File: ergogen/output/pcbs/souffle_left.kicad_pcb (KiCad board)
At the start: 2 copper layers, 167.8 x 99.4 mm, 108 parts

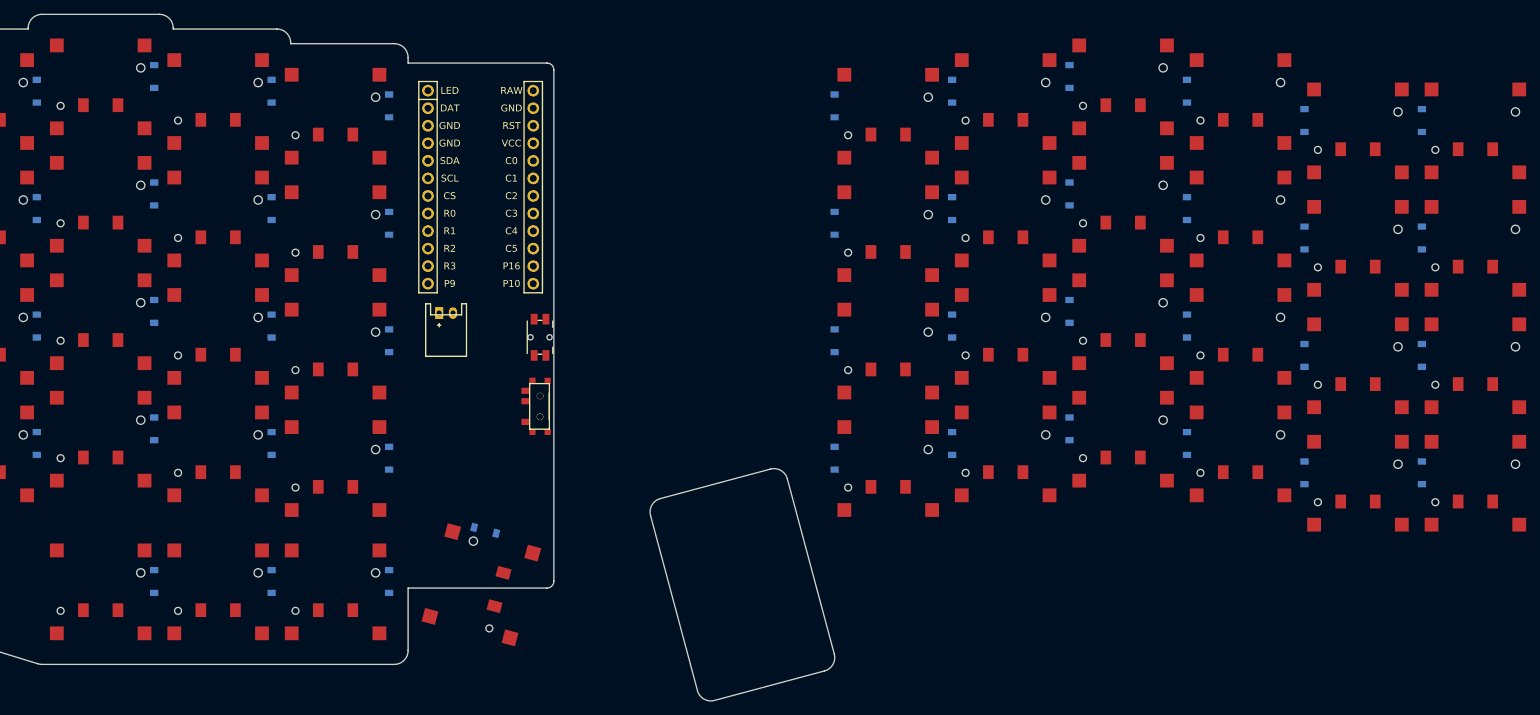
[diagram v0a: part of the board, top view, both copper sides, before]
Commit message: feat: both hands working
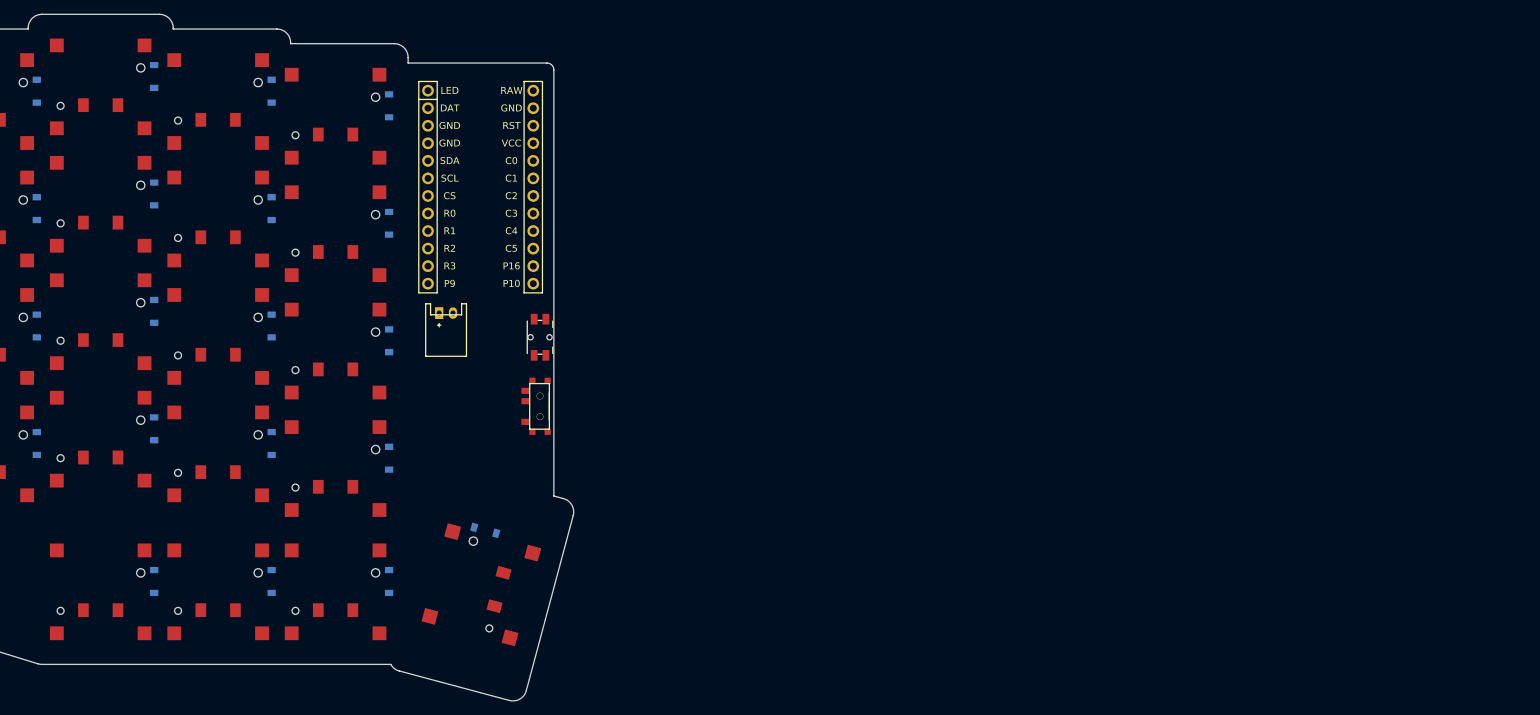
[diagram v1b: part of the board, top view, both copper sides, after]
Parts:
- removed D29, D30, D31, D32, D33, D34, D35, D36, D37, D38, D39, D40, D41, D42, D43, D44, D45, D46, D47, D48, D49, D50, D51, D52: , ceoloide:diode_tht_sod123
- removed S29, S30, S31, S32, S33, S34, S35, S36, S37, S38, S39, S40, S41, S42, S43, S44, S45, S46, S47, S48, S49, S50, S51, S52: , CPG1316S01D02_mikeholscher
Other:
- board size 167.8 x 99.4 mm -> 130 x 99.4 mm

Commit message: feat: choc version
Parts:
- S1, S10, S11, S12, S13, S14, S15, S16, S17, S18, S19, S2, S20, S21, S22, S23, S24, S25, S26, S27, S28, S3, S4, S5, S6, S7, S8, S9: footprint CPG1316S01D02_mikeholscher -> ceoloide:switch_choc_v1_v2; moved to B.Cu
- moved D28 9.38 mm to (216.0, 107.3), turned to -15 degrees
- moved S28 9.38 mm to (215.5, 115.2), turned to 255 degrees
- moved D24 7.66 mm to (200.2, 43.8), turned to -90 degrees
- moved MCU1 7.66 mm to (213.5, 54.3)
- moved S24 7.66 mm to (192.5, 45.3), turned to 180 degrees
- moved D23 7.57 mm to (200.2, 61.3), turned to -90 degrees
- moved S23 7.57 mm to (192.5, 62.8), turned to 180 degrees
- moved B1 7.52 mm to (222.1, 78.3)
- moved D22 7.52 mm to (200.2, 78.8), turned to -90 degrees
- moved JST1 7.52 mm to (208.5, 74.8)
- moved S22 7.52 mm to (192.5, 80.3), turned to 180 degrees
- moved T1 7.52 mm to (222.1, 88.3)
- moved D27 7.51 mm to (200.2, 114.7), turned to -90 degrees
- moved S27 7.51 mm to (192.5, 116.2), turned to 180 degrees
- moved D21 7.50 mm to (200.2, 96.3), turned to -90 degrees
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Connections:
- S1 pad 1: outer_bottom -> C0
- S1 pad 2: C0 -> outer_bottom
- S10 pad 1: ring_home -> C2
- S10 pad 2: C2 -> ring_home
- S11 pad 1: ring_top -> C2
- S11 pad 2: C2 -> ring_top
- S12 pad 1: ring_number -> C2
- S12 pad 2: C2 -> ring_number
- S13 pad 1: middle_bottom -> C3
- S13 pad 2: C3 -> middle_bottom
- S14 pad 1: middle_home -> C3
- S14 pad 2: C3 -> middle_home
- S15 pad 1: middle_top -> C3
- S15 pad 2: C3 -> middle_top
- S16 pad 1: middle_number -> C3
- S16 pad 2: C3 -> middle_number
- S17 pad 1: index_bottom -> C4
- S17 pad 2: C4 -> index_bottom
- S18 pad 1: index_home -> C4
- S18 pad 2: C4 -> index_home
- S19 pad 1: index_top -> C4
- S19 pad 2: C4 -> index_top
- S2 pad 1: outer_home -> C0
- S2 pad 2: C0 -> outer_home
- S20 pad 1: index_number -> C4
- S20 pad 2: C4 -> index_number
- S21 pad 1: inner_bottom -> C5
- S21 pad 2: C5 -> inner_bottom
- S22 pad 1: inner_home -> C5
- S22 pad 2: C5 -> inner_home
- S23 pad 1: inner_top -> C5
- S23 pad 2: C5 -> inner_top
- S24 pad 1: inner_number -> C5
- S24 pad 2: C5 -> inner_number
- S25 pad 1: inward_home -> C2
- S25 pad 2: C2 -> inward_home
- S26 pad 1: outward_home -> C3
- S26 pad 2: C3 -> outward_home
- S27 pad 1: small_thumbkey_home -> C4
- S27 pad 2: C4 -> small_thumbkey_home
- S28 pad 1: thumbkey_home -> C5
- S28 pad 2: C5 -> thumbkey_home
- S3 pad 1: outer_top -> C0
- S3 pad 2: C0 -> outer_top
- S4 pad 1: outer_number -> C0
- S4 pad 2: C0 -> outer_number
- S5 pad 1: pinky_bottom -> C1
- S5 pad 2: C1 -> pinky_bottom
- S6 pad 1: pinky_home -> C1
- S6 pad 2: C1 -> pinky_home
- S7 pad 1: pinky_top -> C1
- S7 pad 2: C1 -> pinky_top
- S8 pad 1: pinky_number -> C1
- S8 pad 2: C1 -> pinky_number
- S9 pad 1: ring_bottom -> C2
- S9 pad 2: C2 -> ring_bottom
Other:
- board size 130 x 99.4 mm -> 140.1 x 101.8 mm

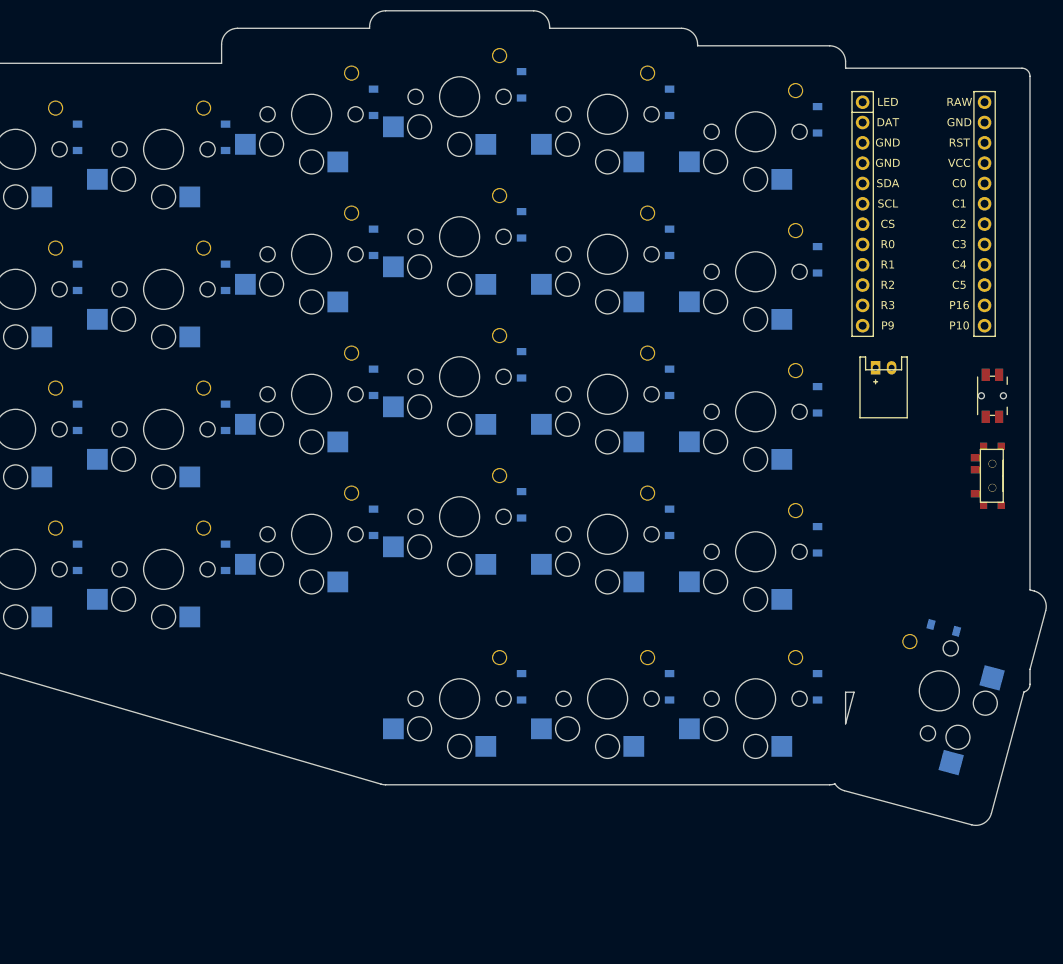
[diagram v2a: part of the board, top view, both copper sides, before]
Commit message: feat: moved mcu to the back and shortened its supporting tab
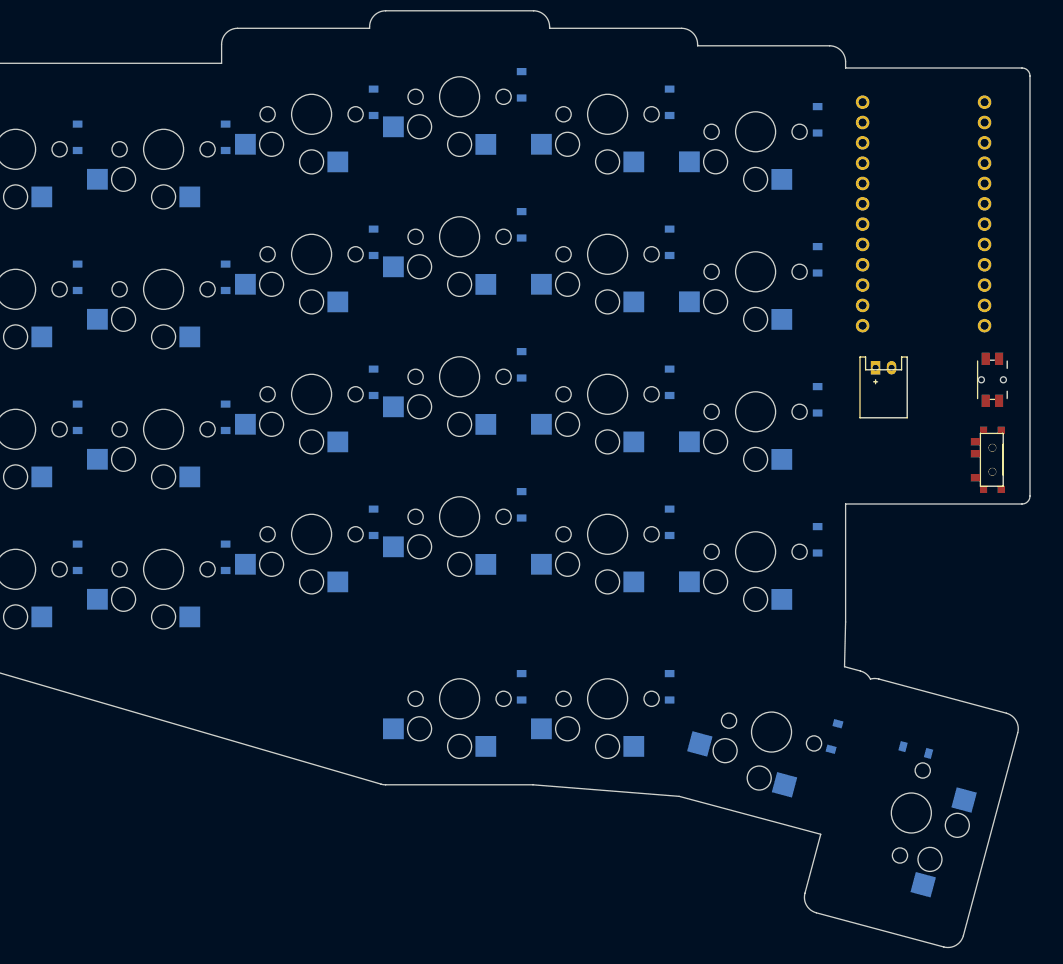
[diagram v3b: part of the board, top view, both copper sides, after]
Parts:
- MCU1: moved to B.Cu
- moved D28 15.7 mm to (212.5, 122.6)
- moved S28 15.7 mm to (212.0, 130.5)
- moved D27 6.56 mm to (202.4, 120.9), turned to -105 degrees
- moved S27 4.61 mm to (194.5, 120.3), turned to 165 degrees
- moved B1 2.00 mm to (222.1, 76.3)
- moved T1 2.00 mm to (222.1, 86.3)
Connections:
- MCU1 pad 1: RAW -> LED
- MCU1 pad 10: C5 -> R2
- MCU1 pad 11: P16 -> R3
- MCU1 pad 12: P10 -> P9
- MCU1 pad 13: P9 -> P10
- MCU1 pad 14: R3 -> P16
- MCU1 pad 15: R2 -> C5
- MCU1 pad 16: R1 -> C4
- MCU1 pad 17: R0 -> C3
- MCU1 pad 18: CS -> C2
- MCU1 pad 19: SCL -> C1
- MCU1 pad 2: GND -> DAT
- MCU1 pad 20: SDA -> C0
- MCU1 pad 21: GND -> VCC
- MCU1 pad 22: GND -> RST
- MCU1 pad 23: DAT -> GND
- MCU1 pad 24: LED -> RAW
- MCU1 pad 3: RST -> GND
- MCU1 pad 4: VCC -> GND
- MCU1 pad 5: C0 -> SDA
- MCU1 pad 6: C1 -> SCL
- MCU1 pad 7: C2 -> CS
- MCU1 pad 8: C3 -> R0
- MCU1 pad 9: C4 -> R1
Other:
- board size 140.1 x 101.8 mm -> 138 x 117.1 mm

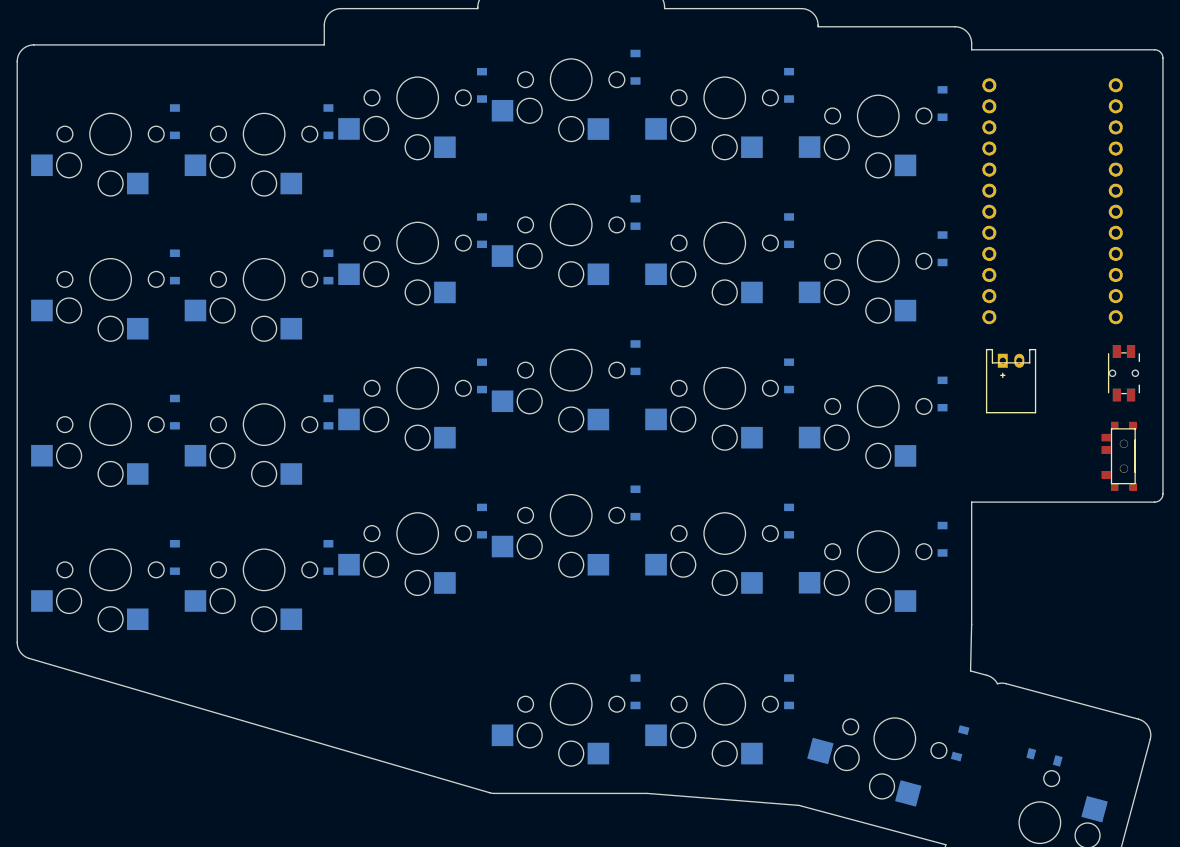
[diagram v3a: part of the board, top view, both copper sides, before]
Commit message: feat: left hand mcu and buttons on the back
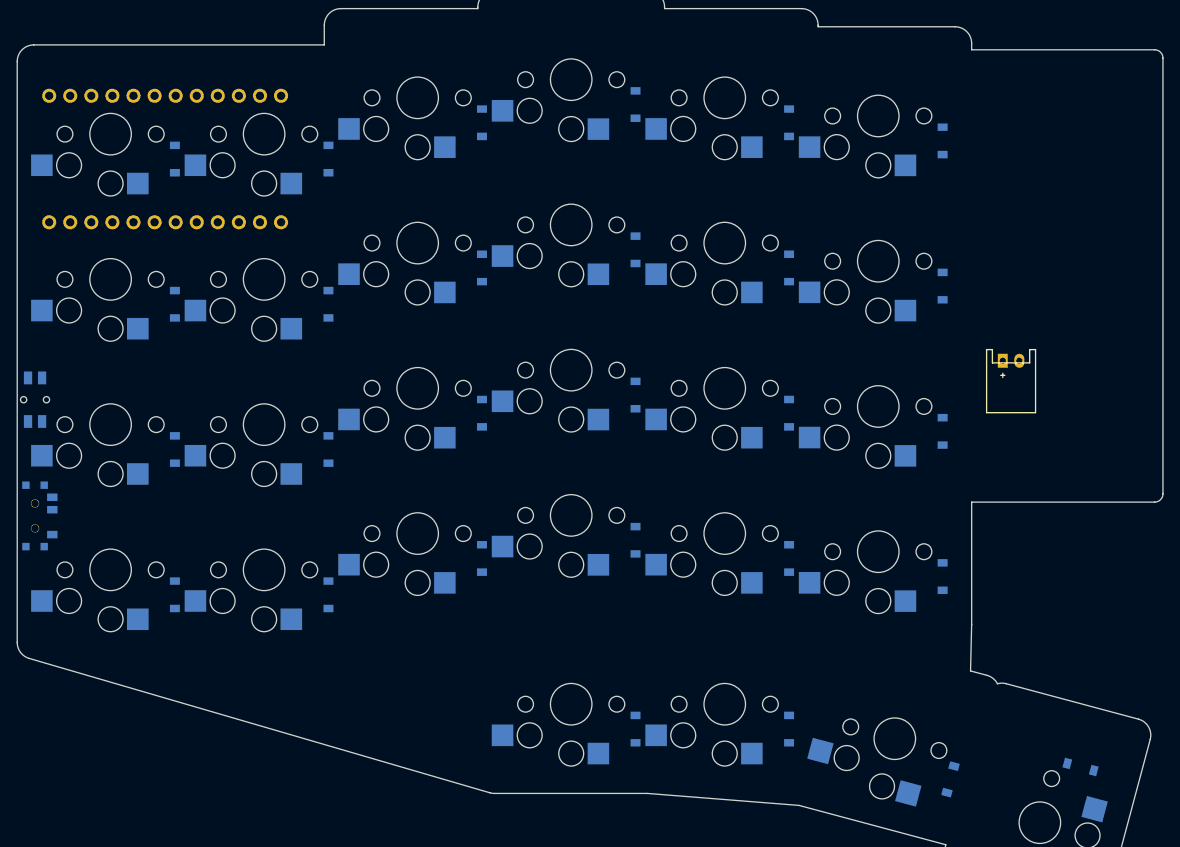
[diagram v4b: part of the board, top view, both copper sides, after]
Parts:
- moved T1 131.4 mm to (90.9, 93.5), turned to 90 degrees
- moved B1 131.2 mm to (90.9, 79.5), turned to 90 degrees
- moved MCU1 108.3 mm to (105.3, 50.5), turned to 90 degrees
- moved D1 4.50 mm to (107.8, 103.0)
- moved D10 4.50 mm to (144.8, 81.1)
- moved D11 4.50 mm to (144.8, 63.6)
- moved D12 4.50 mm to (144.8, 46.1)
- moved D13 4.50 mm to (163.2, 96.4)
- moved D14 4.50 mm to (163.2, 78.9)
- moved D15 4.50 mm to (163.2, 61.4)
- moved D16 4.50 mm to (163.2, 43.9)
- moved D17 4.50 mm to (181.8, 98.6)
- moved D18 4.50 mm to (181.8, 81.1)
- moved D19 4.50 mm to (181.8, 63.6)
- moved D2 4.50 mm to (107.8, 85.5)
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
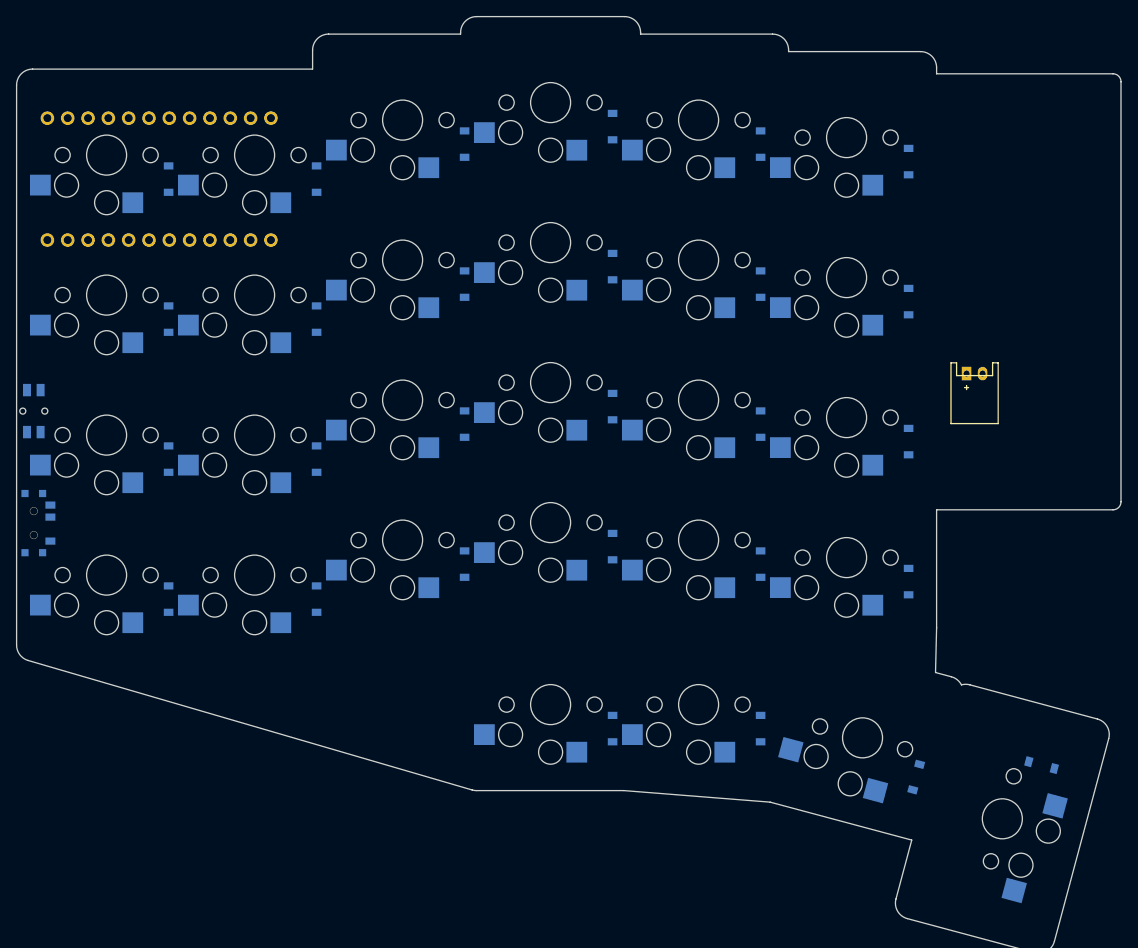
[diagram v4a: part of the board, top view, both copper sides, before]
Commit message: feat: mcu and buttons positioning for the right hand
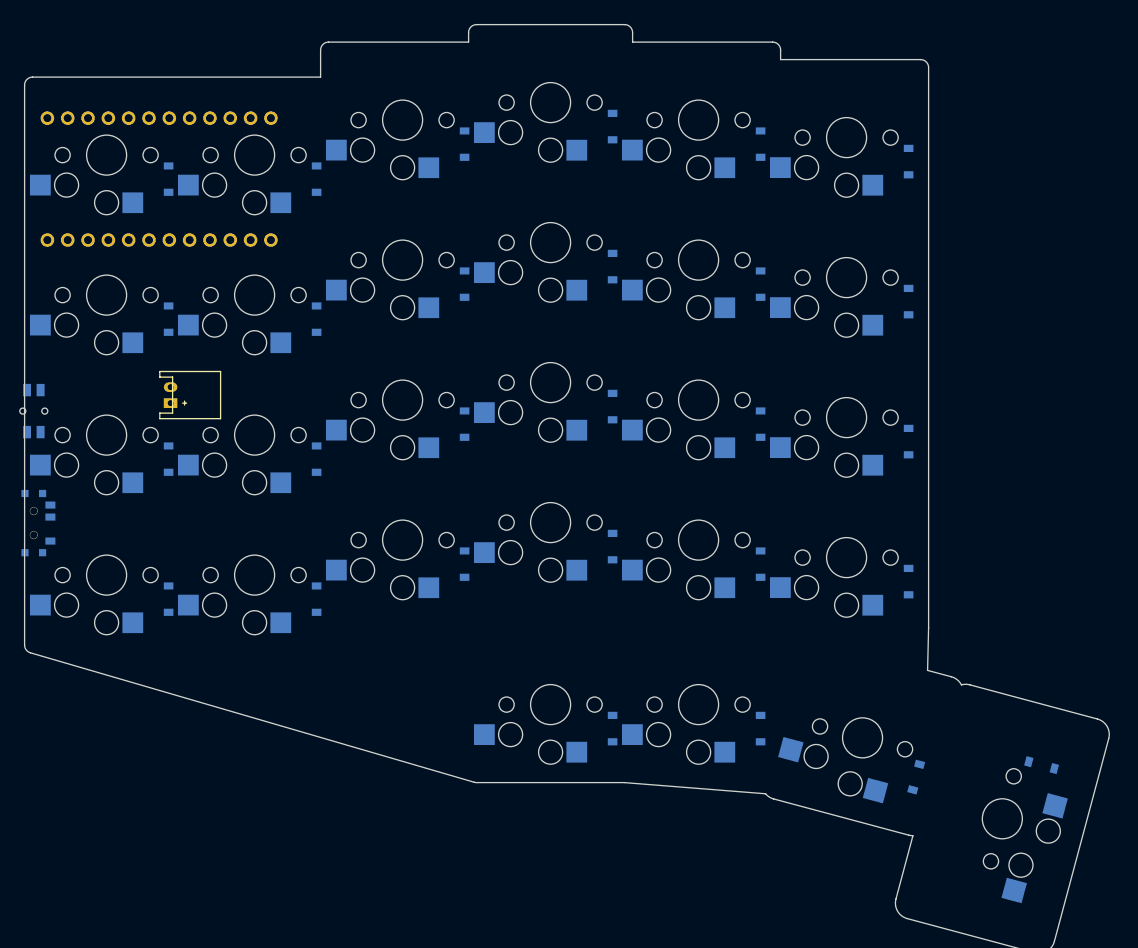
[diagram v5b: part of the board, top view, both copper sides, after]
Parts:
- moved JST1 100.5 mm to (108.0, 77.5), turned to 90 degrees
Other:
- board size 138 x 117.1 mm -> 135.6 x 116.1 mm
